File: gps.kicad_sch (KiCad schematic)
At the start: 57 parts, among them CN6 SQW-104-01-F-D-VS, Q1 DMN62D0U-7, U3 TI TPS79301DBV, U4 TI TPS79301DBV, U7 SN74LVC1G125DBV

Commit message: started on power
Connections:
- net ANT_VCC renamed VCC_ANT
- net GNSS_VCC renamed VCC_GNSS
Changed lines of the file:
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@@
     (effects (font (size 1.27 1.27)) (justify left bottom))
   )
-  (label "GNSS_VCC" (at 233.68 48.26 0) (fields_autoplaced)
+  (label "VCC_GNSS" (at 233.68 48.26 0) (fields_autoplaced)
     (effects (font (size 1.27 1.27)) (justify left bottom))
   )
-  (label "ANT_VCC" (at 204.47 81.28 180) (fields_autoplaced)
+  (label "VCC_ANT" (at 204.47 81.28 180) (fields_autoplaced)
     (effects (font (size 1.27 1.27)) (justify right bottom))
   )
@@
     (effects (font (size 1.27 1.27)) (justify right bottom))
   )
-  (label "GNSS_VCC" (at 248.92 118.11 0) (fields_autoplaced)
+  (label "VCC_GNSS" (at 248.92 118.11 0) (fields_autoplaced)
     (effects (font (size 1.27 1.27)) (justify left bottom))
   )
@@
     (effects (font (size 1.27 1.27)) (justify right bottom))
   )
-  (label "ANT_VCC" (at 233.68 45.72 0) (fields_autoplaced)
+  (label "VCC_ANT" (at 233.68 45.72 0) (fields_autoplaced)
     (effects (font (size 1.27 1.27)) (justify left bottom))
   )
-  (label "GNSS_VCC" (at 229.87 45.72 180) (fields_autoplaced)
+  (label "VCC_GNSS" (at 229.87 45.72 180) (fields_autoplaced)
     (effects (font (size 1.27 1.27)) (justify right bottom))
   )

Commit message: Schematic mostly done
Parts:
- removed R22: 68k, Resistor_SMD:R_0402_1005Metric, symbol Auto_Library_WUT:KOA Speer RK73H1ETTP6802F
- removed R23: 22k, Resistor_SMD:R_0402_1005Metric, symbol Auto_Library_WUT:KOA Speer RK73H1ETTP2202F
- added F2: 250mA, Fuse:Fuse_0603_1608Metric, symbol Fuse_WUT:Littelfuse_0467.250NR
- added LD5: Green, LED_SMD:LED_0603_1608Metric, symbol Auto_Library_WUT:Ekinglux_E6C0603VGAC1UDA
- added R22: 20k, Resistor_SMD:R_0402_1005Metric, symbol Auto_Library_WUT:KOA Speer RK73H1ETTP2002F
- added R23: 6k8, Resistor_SMD:R_0402_1005Metric, symbol Auto_Library_WUT:KOA Speer RK73H1ETTP6801F
- added R84: 4k7, Resistor_SMD:R_0402_1005Metric, symbol Auto_Library_WUT:KOA Speer RK73H1ETTP4701F
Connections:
- net 0V: now also LD5.1 (K), R23.2
- net at C18.1, FB7.1, TP2.1: now also F2.2, R84.1; no longer C14.1, C16.1, U4.6 (OUT)
- net 5V0_PI: now reaches C4.1, L1.1
- net at C14.2, U4.5 (FB): now also R22.2, R23.1
- new net: C14.1, C16.1, F2.1, R22.1, U4.6 (OUT)
- new net: LD5.2 (A), R84.2
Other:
- note added: "Vfb = 1.225V Vout = 1.225 * (1+20/6.8) = 4.83V Dropout = 140mV @ 5Vin, 125C (worst case)"
- note removed: "TODO Input voltage"
- note removed: "Vfb = 1.225V Vout = 1.225 * (1+68/22) = 5.01V"
- moved on the sheet: C18, C19, FB7, TP2

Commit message: schematic complete
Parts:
- removed R24: 100R, Resistor_SMD:R_0402_1005Metric, symbol Auto_Library_WUT:KOA Speer RK73H1ETTP1000F
- added C121, C144, C159: 100n, Capacitor_SMD:C_0402_1005Metric, symbol Auto_Library_WUT:Yageo CC0402KRX7R8BB104
- added FB30, FB31: 1k8, Inductor_SMD:L_0402_1005Metric, symbol Auto_Library_WUT:Murata BLM15BD182SN1D
- added H7: CAB.0101, symbol Accessories_WUT:Taoglas_CAB.0101
- added OSC1: 10MHz, Crystal:Crystal_SMD_3225-4Pin_3.2x2.5mm, symbol Oscillator_WUT:Abracon_I537-2O7-10.000_MHz
- added R133, R134, R135: 33R, Resistor_SMD:R_0402_1005Metric, symbol Auto_Library_WUT:KOA Speer RK73H1ETTP33R0F
- added R137: 10k, Resistor_SMD:R_0402_1005Metric, symbol Auto_Library_WUT:KOA Speer RK73H1ETTP1002F
- added U16: SN74LVC2G157DCU, Package_SO:VSSOP-8_2.3x2mm_P0.5mm, symbol Logic_WUT:TI_SN74LVC2G157DCU
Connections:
- net 0V: now also C121.2, C144.2, C159.2, OSC1.1 (GND), OSC1.2 (GND), R137.2, U16.4 (GND), U16.7 (~{G})
- net GNSS_RESET: now also C23.1, Q1.1 (G), R25.1
- net GNSS_25MHZ renamed GNSS_CLK
- net GNSS_CLK: no longer R17.1
- new net: C144.1, FB31.1, OSC1.4 (VCC)
- new net: R134.2, U16.3 (~{Y})
- new net: C121.1, FB30.1, U16.8 (VCC)
- new net: R135.1, U16.1 (A)
- new net: R17.1, U16.2 (B)
- new net: R133.2, U16.5 (Y)
- new net: OSC1.3 (OUT), R135.2
- new net 3V3: FB30.2, FB31.2
- new net CLK_SEL: C159.1, R137.1, U16.6 (~{A}/B)
- new net REF_CLK_N: R134.1
- new net REF_CLK_P: R133.1
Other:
- moved on the sheet: C10, C11, C118, C119, C12, C13, C14, C15, C16, C17, C18, C19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

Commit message: Moved to preferred library
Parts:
- C10, C118, C121, C144, C159, C18, C21, C23, C9: symbol Auto_Library_WUT:Yageo CC0402KRX7R8BB104 -> Preferred_WUT:Yageo CC0402KRX7R8BB104
- C15, C16, C17, C4, C7, C8: symbol Auto_Library_WUT:Samsung Electro-Mechanics CL10A106MO8NQNC -> Preferred_WUT:Samsung Electro-Mechanics CL10A106MO8NQNC
- FB2, FB24, FB3, FB30, FB31, FB4, FB5, FB7: symbol Auto_Library_WUT:Murata BLM15BD182SN1D -> Preferred_WUT:Murata BLM15BD182SN1D
- FB6: symbol Auto_Library_WUT:Murata BLM18AG601SN1D -> Preferred_WUT:Murata BLM18AG601SN1D
- LD5: symbol Auto_Library_WUT:Ekinglux_E6C0603VGAC1UDA -> Preferred_WUT:Ekinglux_E6C0603VGAC1UDA
- R133, R134, R135, R16, R17, R18, R19: symbol Auto_Library_WUT:KOA Speer RK73H1ETTP33R0F -> Preferred_WUT:KOA Speer RK73H1ETTP33R0F
- R137, R25, R27: symbol Auto_Library_WUT:KOA Speer RK73H1ETTP1002F -> Preferred_WUT:KOA Speer RK73H1ETTP1002F
- R26: symbol Auto_Library_WUT:KOA Speer RK73H1ETTP1000F -> Preferred_WUT:KOA Speer RK73H1ETTP1000F

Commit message: Started placement
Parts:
- removed C19, C24: 4n7, Capacitor_SMD:C_0603_1608Metric, symbol Auto_Library_WUT:Kemet C0603C472J3GACTU
- removed C20: 68u, Capacitor_WUT:Wurth_WCAP_PSHP_8x8.7mm_SM, symbol Auto_Library_WUT:Wurth Elektronik_875115452001
- removed C4: 10u, Capacitor_SMD:C_0603_1608Metric, symbol Preferred_WUT:Samsung Electro-Mechanics CL10A106MO8NQNC
- removed L1: 4u7, Inductor_SMD:L_1210_3225Metric, symbol Auto_Library_WUT:Bourns DFE322512F-4R7M=P2
- added C19, C4: 4n7, Capacitor_SMD:C_0402_1005Metric, symbol Auto_Library_WUT:Kemet C0402C472K5RACTU
- added C20: 10u, Capacitor_SMD:C_0603_1608Metric, symbol Preferred_WUT:Samsung Electro-Mechanics CL10A106MO8NQNC
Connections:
- net 0V: now also C19.2, C20.2, C4.2
- net 5V0_PI: now also C7.1, C8.1, U3.1 (IN), U3.3 (EN), U4.1 (IN), U4.3 (EN)
- net GNSS_PPS: no longer C11.1, CN6.6 (Pin_6), FB4.2
- net GNSS_RX: now also R18.2; no longer C6.1, CN6.5 (Pin_5), FB2.1, FB3.2
- net GNSS_TX: now also FB3.1; no longer C5.1, CN6.3 (Pin_3), FB2.2, R18.1
- net VCC_ANT: now also C19.1
- net VCC_GNSS: now also C20.1
- net at U16.1 (A): now also R17.1; no longer R135.1
- net at U16.2 (B): now also R135.1; no longer R17.1
- net GNSS_CLK renamed GNSS_CLK_M
- net ~{GNSS_RESET} renamed ~{GNSS_RESET_M}
- net ~{GNSS_RESET_M}: now also C4.1
- new net: FB2.1, R18.1
- new net GNSS_PPS_M: C11.1, CN6.6 (Pin_6), FB4.2
- new net GNSS_RX_M: C6.1, CN6.5 (Pin_5), FB3.2
- new net GNSS_TX_M: C5.1, CN6.3 (Pin_3), FB2.2
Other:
- moved on the sheet: C12, C144, FB31, FB5, OSC1, R135, R17

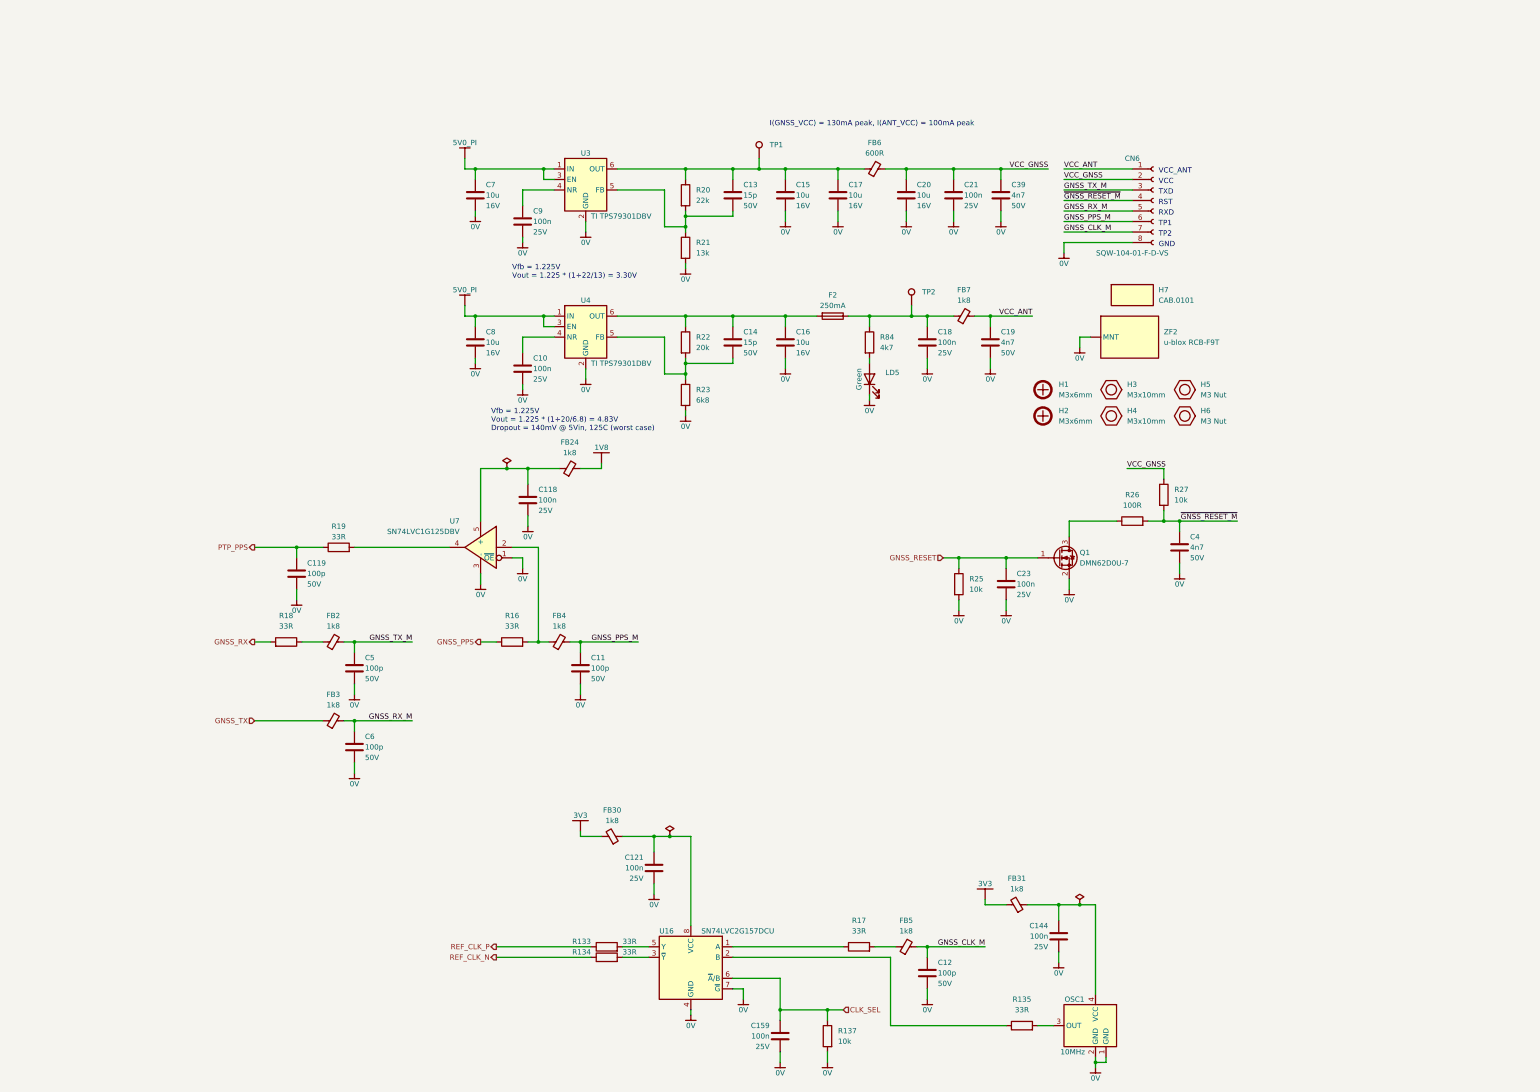
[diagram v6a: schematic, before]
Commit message: moving to discrete GPS recevier
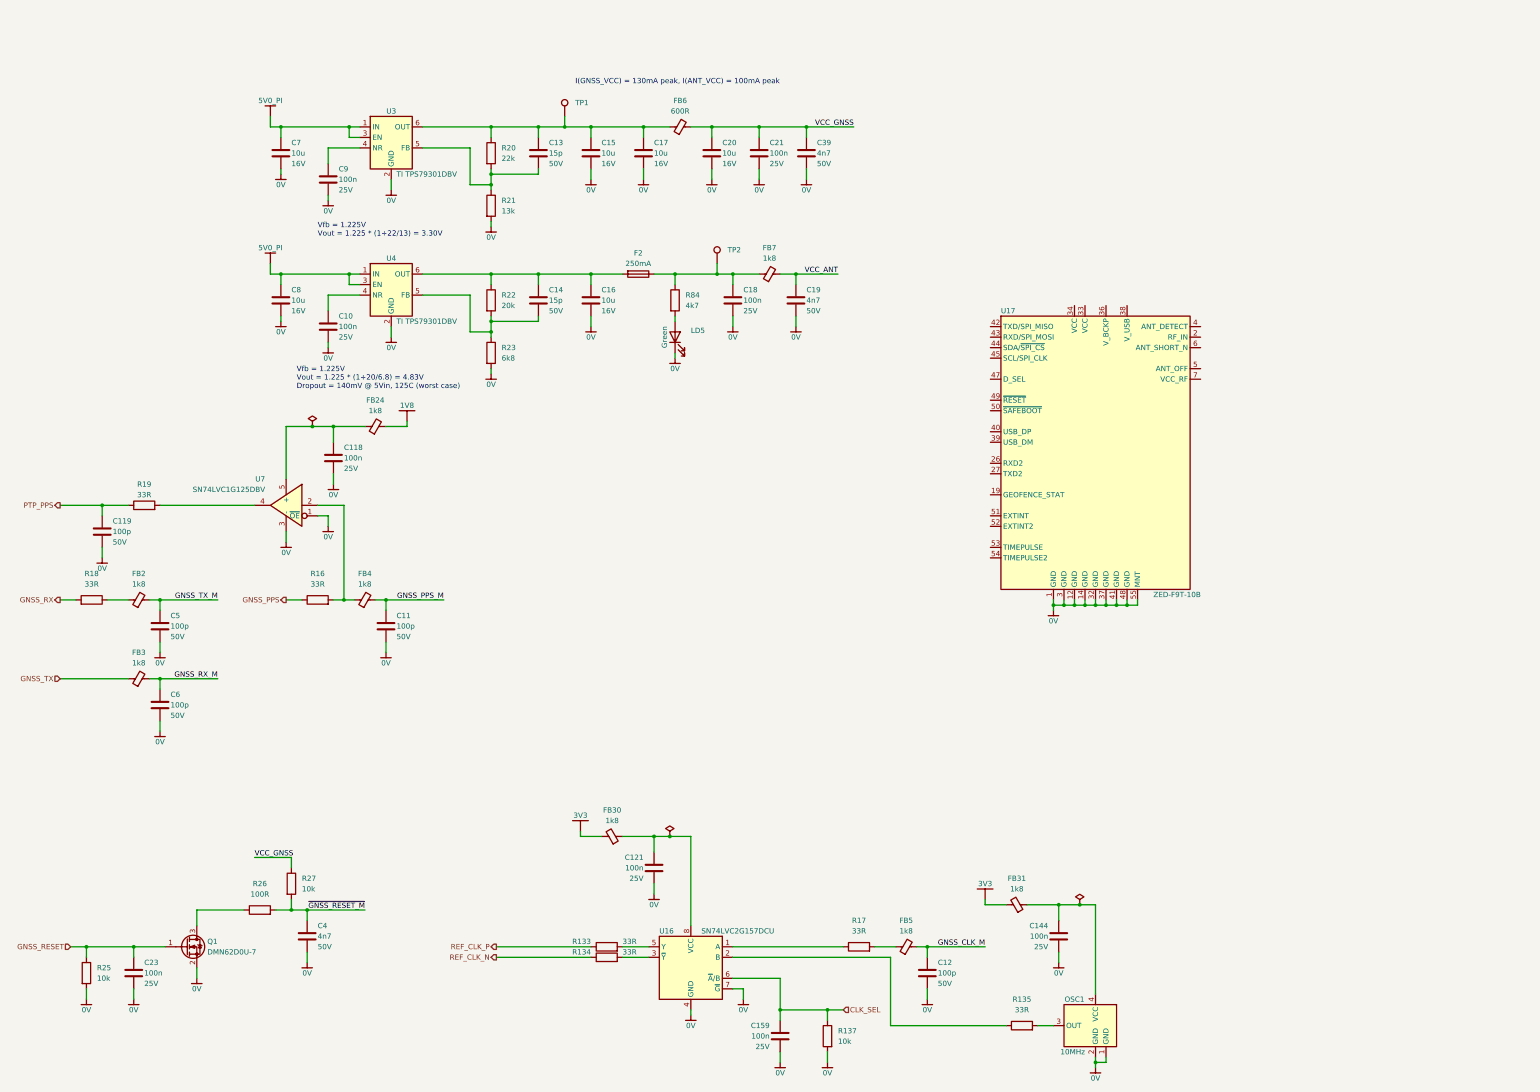
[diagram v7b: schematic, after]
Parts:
- removed CN6: SQW-104-01-F-D-VS, Connector_WUT:Samtec_SQW-104-01, symbol Connector_WUT:Samtec_SQW-104-01-F-D-VS
- removed H1, H2: M3x6mm, symbol Accessories_WUT:TR_M36_PRA2MCS100-_
- removed H3, H4: M3x10mm, symbol Accessories_WUT:Wurth_971100324
- removed H5, H6: M3 Nut, symbol Accessories_WUT:TR_M3-_HFA2-S100-
- removed H7: CAB.0101, symbol Accessories_WUT:Taoglas_CAB.0101
- removed ZF2: u-blox RCB-F9T, RF_WUT:u-blox_RCB-F9T, symbol Modules_WUT:u-blox_RCB-F9T
- added U17: ZED-F9T-10B, RF_WUT:uBlox_ZED, symbol RF_WUT:uBlox_ZED-F9T-10B
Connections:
- net 0V: now also U17.1 (GND), U17.12 (GND), U17.14 (GND), U17.3 (GND), U17.32 (GND), U17.37 (GND), U17.41 (GND), U17.48 (GND), U17.55 (MNT)
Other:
- note removed: "GND"
- note removed: "RST"
- note removed: "RXD"
- note removed: "TP1"
- note removed: "TP2"
- note removed: "TXD"
- note removed: "VCC"
- note removed: "VCC_ANT"
- moved on the sheet: C10, C11, C118, C119, C13, C14, C15, C16, C17, C18, C19, C20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

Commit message: Moved to discrete GPS
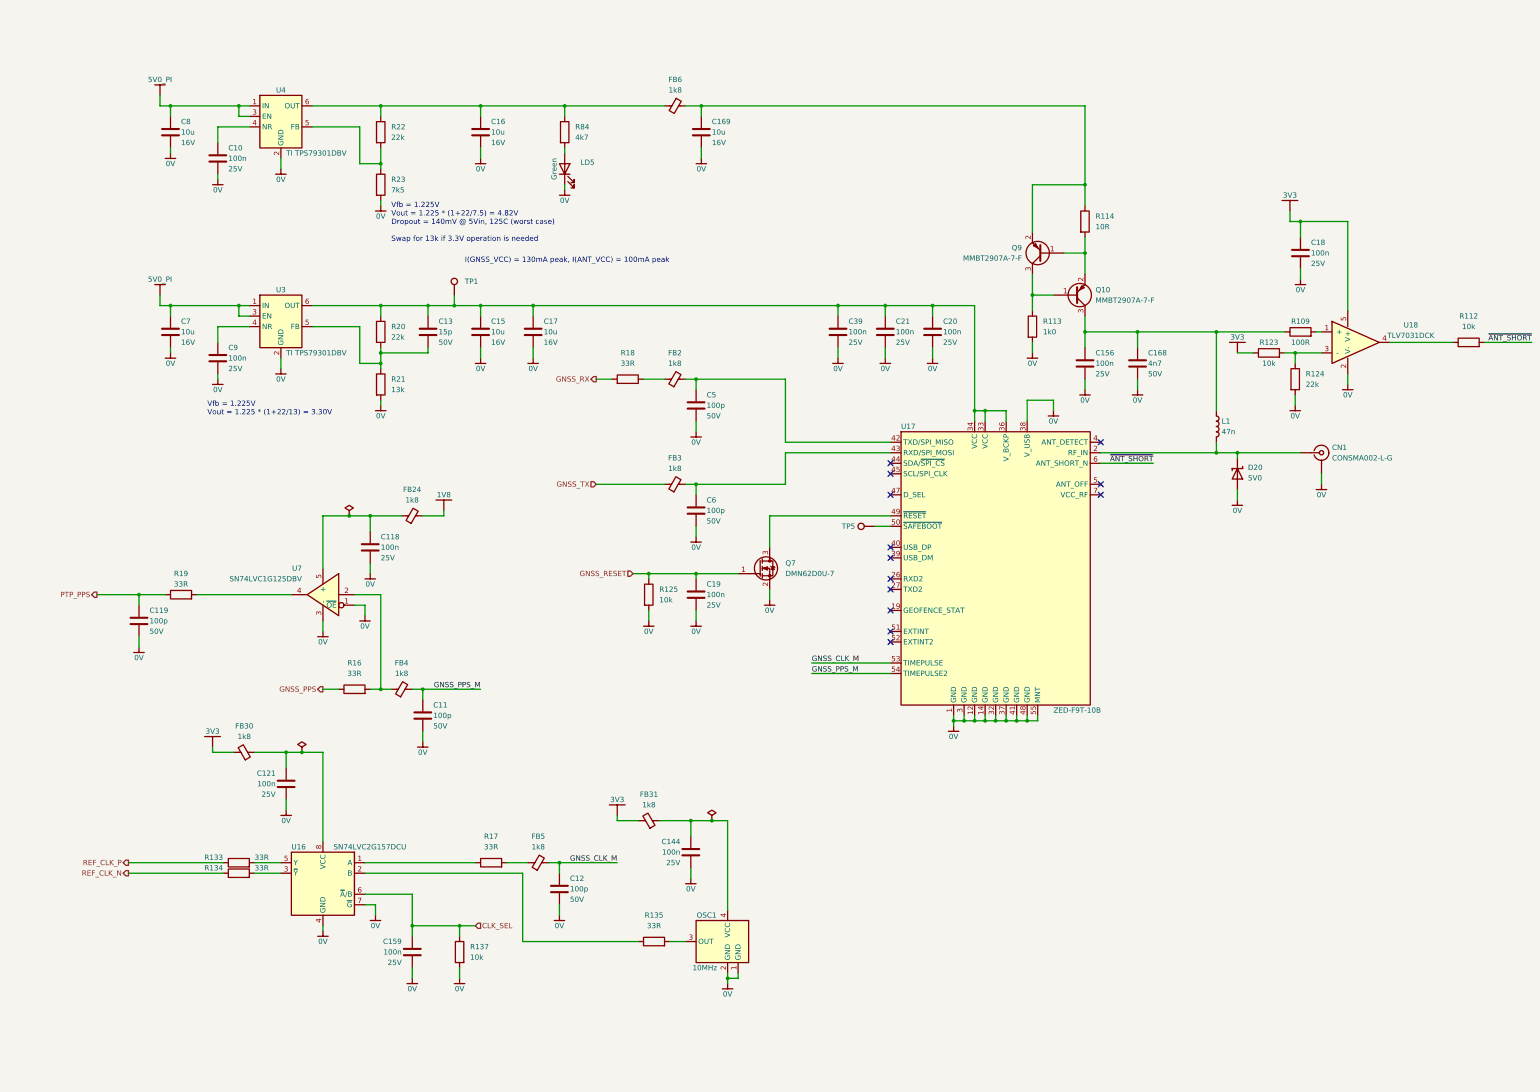
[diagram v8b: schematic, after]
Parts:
- removed C14: 15p, Capacitor_SMD:C_0402_1005Metric, symbol Auto_Library_WUT:Kemet C0402C150D5GACTU
- removed C19, C39, C4: 4n7, Capacitor_SMD:C_0402_1005Metric, symbol Auto_Library_WUT:Kemet C0402C472K5RACTU
- removed C20: 10u, Capacitor_SMD:C_0603_1608Metric, symbol Preferred_WUT:Samsung Electro-Mechanics CL10A106MO8NQNC
- removed C23: 100n, Capacitor_SMD:C_0402_1005Metric, symbol Preferred_WUT:Yageo CC0402KRX7R8BB104
- removed F2: 250mA, Fuse:Fuse_0603_1608Metric, symbol Fuse_WUT:Littelfuse_0467.250NR
- removed FB6: 600R, Inductor_SMD:L_0603_1608Metric, symbol Preferred_WUT:Murata BLM18AG601SN1D
- removed FB7: 1k8, Inductor_SMD:L_0402_1005Metric, symbol Preferred_WUT:Murata BLM15BD182SN1D
- removed Q1: DMN62D0U-7, Package_TO_SOT_SMD:SOT-23, symbol FET_WUT:DMN62D0U-7
- removed R22: 20k, Resistor_SMD:R_0402_1005Metric, symbol Auto_Library_WUT:KOA Speer RK73H1ETTP2002F
- removed R23: 6k8, Resistor_SMD:R_0402_1005Metric, symbol Auto_Library_WUT:KOA Speer RK73H1ETTP6801F
- removed R25, R27: 10k, Resistor_SMD:R_0402_1005Metric, symbol Preferred_WUT:KOA Speer RK73H1ETTP1002F
- removed R26: 100R, Resistor_SMD:R_0402_1005Metric, symbol Preferred_WUT:KOA Speer RK73H1ETTP1000F
- removed TP2: ~, TestPoint:TestPoint_Pad_D1.0mm, symbol Layout_WUT:TestPoint_1mm_SMD
- added C156, C19, C20, C39: 100n, Capacitor_SMD:C_0402_1005Metric, symbol Preferred_WUT:Yageo CC0402KRX7R8BB104
- added C168: 4n7, Capacitor_SMD:C_0402_1005Metric, symbol Auto_Library_WUT:Kemet C0402C472K5RACTU
- added C169: 10u, Capacitor_SMD:C_0603_1608Metric, symbol Preferred_WUT:Samsung Electro-Mechanics CL10A106MO8NQNC
- added CN1: CONSMA002-L-G, Connector_WUT:SMA_Linx_CONSMA002-L-G_Horizontal, symbol Connector_WUT:TE-Connectivity_CONSMA002-L-G
- added D20: 5V0, Diode_SMD:D_SOD-523, symbol Preferred_WUT:Littelfuse AQ3522-01LTG
- added FB6: 1k8, Inductor_SMD:L_0402_1005Metric, symbol Preferred_WUT:Murata BLM15BD182SN1D
- added L1: 47n, Inductor_SMD:L_0402_1005Metric, symbol Auto_Library_WUT:Coilcraft 0402DC-47NXJRW
- added Q10, Q9: MMBT2907A-7-F, Package_TO_SOT_SMD:SOT-23, symbol Transistor_WUT:Diodes-Inc_MMBT2907A-7-F
- added Q7: DMN62D0U-7, Package_TO_SOT_SMD:SOT-23, symbol Transistor_WUT:Diodes-Inc_DMN62D0U-7
- added R109: 100R, Resistor_SMD:R_0402_1005Metric, symbol Preferred_WUT:KOA Speer RK73H1ETTP1000F
- added R112, R123, R125: 10k, Resistor_SMD:R_0402_1005Metric, symbol Preferred_WUT:KOA Speer RK73H1ETTP1002F
- added R113: 1k0, Resistor_SMD:R_0402_1005Metric, symbol Preferred_WUT:KOA Speer RK73H1ETTP1001F
- added R114: 10R, Resistor_SMD:R_0805_2012Metric, symbol Auto_Library_WUT:KOA Speer RK73H2ATTD10R0F
- added R124, R22: 22k, Resistor_SMD:R_0402_1005Metric, symbol Auto_Library_WUT:KOA Speer RK73H1ETTP2202F
- added R23: 7k5, Resistor_SMD:R_0402_1005Metric, symbol Auto_Library_WUT:KOA Speer RK73H1ETTP7501F
- added TP5: ~, TestPoint:TestPoint_Pad_D1.0mm, symbol Layout_WUT:TestPoint_1mm_SMD
- added U18: TLV7031DCK, Package_TO_SOT_SMD:SOT-353_SC-70-5, symbol IC_WUT:TLV7031DCK
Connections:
- net GNSS_RX_M is gone; now on an unnamed net: C6.1, FB3.2
- net GNSS_TX_M is gone; now on an unnamed net: C5.1, FB2.2
- net VCC_GNSS is gone; now on an unnamed net: C21.1
- net 0V: now also U17.38 (V_USB), C156.2, C168.2, C169.2, C19.2, C20.2, C39.2, CN1.2 (Ext), D20.2 (A), Q7.2 (S), R113.2, R124.2, R125.2, R23.2, U18.2 (V-)
- net 3V3: now also C18.1, R123.1, U18.5 (V+)
- net GNSS_CLK_M: now also U17.53 (TIMEPULSE)
- net GNSS_PPS_M: now also U17.54 (TIMEPULSE2)
- net GNSS_RESET: now also C19.1, Q7.1 (G), R125.1
- net at C13.1, C15.1, C17.1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: now also U17.33 (VCC), U17.34 (VCC), U17.36 (V_BCKP), C20.1, C39.1
- net at R84.1: now also C16.1, U4.6 (OUT), FB6.2, R22.1; no longer C18.1
- net at U4.5 (FB): now also R22.2, R23.1
- net at U17.2 (RF_IN): now also CN1.1 (In), D20.1 (K), L1.2
- net at U17.49 (~{RESET}): now also Q7.3 (D)
- net at U17.50 (~{SAFEBOOT}): now also TP5.1
- net ~{ANT_SHORT}: now reaches U17.6 (ANT_SHORT_N)
- net ~{ANT_SHORT}: now also R112.2
- new net: C156.1, C168.1, L1.1, Q10.3 (C), R109.1
- new net: R112.1, U18.4
- new net: C169.1, FB6.1, Q9.2 (E), R114.1
- new net: Q10.1 (B), Q9.3 (C), R113.1
- new net: Q10.2 (E), Q9.1 (B), R114.2
- new net: R109.2, U18.1 (+)
- new net: R123.2, R124.1, U18.3 (-)
- no-connect marks 0 -> 13
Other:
- note added: "Vfb = 1.225V Vout = 1.225 * (1+22/7.5) = 4.82V Dropout = 140mV @ 5Vin, 125C (worst case) Swap for 13k if 3.3V operation is needed"
- note removed: "Vfb = 1.225V Vout = 1.225 * (1+20/6.8) = 4.83V Dropout = 140mV @ 5Vin, 125C (worst case)"
- moved on the sheet: C10, C11, C118, C119, C12, C121, C13, C144, C15, C159, C16, C17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
